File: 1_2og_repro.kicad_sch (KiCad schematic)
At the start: 217 parts, among them J1 Conn_01x03, J2 USB_B_Mini, J3 Conn_01x03, Q1 2N7002, SW1 MX_SW_solder, SW10 MX_SW_solder, SW11 MX_SW_solder, SW12 MX_SW_solder, SW13 MX_SW_solder, SW14 MX_SW_solder, SW15 MX_SW_solder, SW16 MX_SW_solder, SW17 MX_SW_solder, SW18 MX_SW_solder, SW19 MX_SW_solder, SW2 MX_SW_solder, SW20 MX_SW_solder, SW21 MX_SW_solder, SW22 MX_SW_solder, SW23 MX_SW_solder, SW24 MX_SW_solder, SW25 MX_SW_solder, SW26 MX_SW_solder, SW27 MX_SW_solder, SW28 MX_SW_solder, SW29 MX_SW_solder, SW3 MX_SW_solder, SW30 MX_SW_solder, SW31 MX_SW_solder, SW32 MX_SW_solder, SW33 MX_SW_solder, SW34 MX_SW_solder, SW35 MX_SW_solder, SW36 MX_SW_solder, SW37 MX_SW_solder, SW38 MX_SW_solder, SW39 MX_SW_solder, SW4 MX_SW_solder, SW40 MX_SW_solder, SW41 MX_SW_solder, SW42 MX_SW_solder, SW43 MX_SW_solder, SW44 MX_SW_solder, SW45 MX_SW_solder, SW46 MX_SW_solder, SW47 MX_SW_solder, SW48 MX_SW_solder, SW49 MX_SW_solder, SW5 MX_SW_solder, SW50 MX_SW_solder, SW51 MX_SW_solder, SW52 MX_SW_solder, SW53 MX_SW_solder, SW54 MX_SW_solder, SW55 MX_SW_solder, SW56 MX_SW_solder, SW57 MX_SW_solder, SW58 MX_SW_solder, SW59 MX_SW_solder, SW6 MX_SW_solder, SW60 MX_SW_solder, SW61 MX_SW_solder, SW62 MX_SW_solder, SW63 MX_SW_solder, SW64 MX_SW_solder, SW65 MX_SW_solder, SW66 MX_SW_solder, SW67 MX_SW_solder, SW68 MX_SW_solder, SW69 MX_SW_solder, SW7 MX_SW_solder, SW70 MX_SW_solder, SW71 MX_SW_solder, SW72 MX_SW_solder, SW73 MX_SW_solder, SW74 MX_SW_solder, SW75 MX_SW_solder, SW76 MX_SW_solder, SW77 MX_SW_solder, SW78 MX_SW_solder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

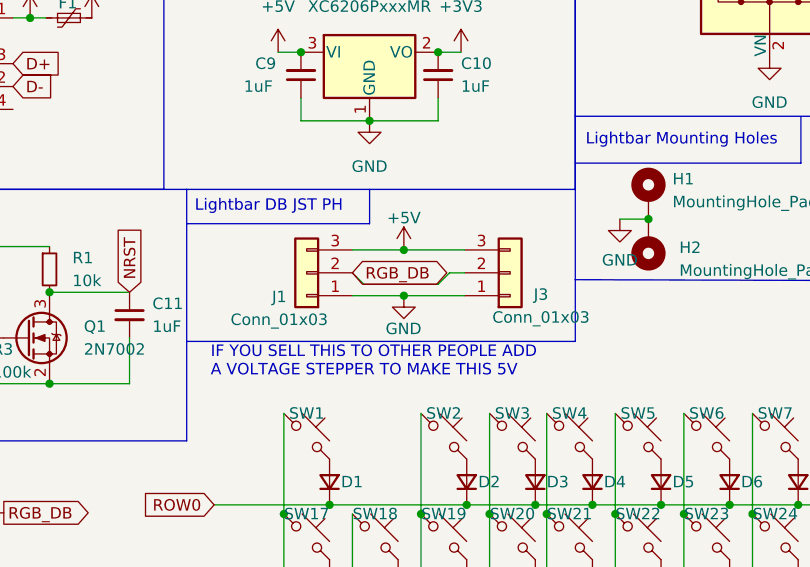
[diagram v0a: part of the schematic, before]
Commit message: add lightbar kinda (gerbers have not been fully updated yet, bom is broken)
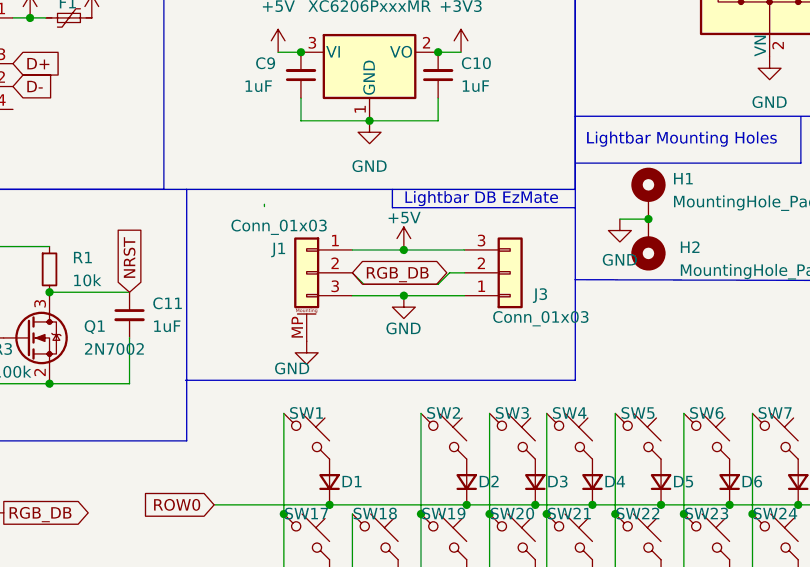
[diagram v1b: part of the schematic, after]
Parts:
- J1: footprint Connector_JST:JST_PH_S3B-PH-K_1x03_P2.00mm_Horizontal -> Connector_Molex:Molex_Pico-EZmate_78171-0003_1x03-1MP_P1.20mm_Vertical; symbol Connector_Generic:Conn_01x03 -> Connector_Generic_MountingPin:Conn_01x03_MountingPin
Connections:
- net +5V: now also J1.1 (Pin_1); no longer J1.3 (Pin_3)
- net GND: now also J1.3 (Pin_3), J1.MP (MountPin); no longer J1.1 (Pin_1)
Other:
- note added: "Lightbar DB EzMate"
- note removed: "IF YOU SELL THIS TO OTHER PEOPLE ADD A VOLTAGE STEPPER TO MAKE THIS 5V"
- note removed: "Lightbar DB JST PH"
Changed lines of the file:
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@@
     (stroke (width 0) (type default))
   )
-  (polyline (pts (xy 156.845 74.676) (xy 156.845 67.818))
+  (polyline (pts (xy 156.845 78.994) (xy 156.845 67.818))
     (stroke (width 0) (type default))
   )
@@
     (stroke (width 0) (type default))
   )
-  (polyline (pts (xy 133.985 61.595) (xy 133.985 57.785))
+  (polyline (pts (xy 136.525 59.817) (xy 136.525 57.785))
     (stroke (width 0) (type default))
   )
@@
     (stroke (width 0) (type default))
   )
-  (polyline (pts (xy 156.845 74.676) (xy 113.665 74.676))
+  (polyline (pts (xy 156.845 78.994) (xy 113.538 78.994))
     (stroke (width 0) (type default))
   )
@@
     (stroke (width 0) (type default))
   )
+  (wire (pts (xy 122.301 59.436) (xy 122.301 59.69))
+    (stroke (width 0) (type default))
+  )
   (wire (pts (xy 80.645 23.495) (xy 90.805 23.495))
     (stroke (width 0) (type default))
@@
     (stroke (width 0) (type default))
   )
-  (polyline (pts (xy 113.665 61.595) (xy 133.985 61.595))
+  (polyline (pts (xy 136.525 59.817) (xy 156.845 59.817))
     (stroke (width 0) (type default))
   )
@@
     (effects (font (size 1.27 1.27)) (justify left bottom))
   )
-  (text "IF YOU SELL THIS TO OTHER PEOPLE ADD\nA VOLTAGE STEPPER TO MAKE THIS 5V"
-    (at 116.332 78.74 0)
-    (effects (font (size 1.27 1.27)) (justify left bottom))
-  )
   (text "Voltage Regulator" (at 112.395 33.655 0)
     (effects (font (size 1.27 1.27)) (justify left bottom))
@@
     (effects (font (size 1.27 1.27)) (justify left bottom))
   )
-  (text "Lightbar DB JST PH" (at 114.554 60.452 0)
+  (text "Lightbar DB EzMate" (at 137.795 59.69 0)
     (effects (font (size 1.27 1.27)) (justify left bottom))
   )
@@
     )
   )
+  (symbol (lib_name "GND_1") (lib_id "power:GND") (at 127 74.676 0) (mirror y) (unit 1)
+    (in_bom yes) (on_board yes) (dnp no)
+    (property "Reference" "#PWR020" (at 127 81.026 0)
+      (effects (font (size 1.27 1.27)) hide)
+    )
+    (property "Value" "GND" (at 127.381 77.724 0)
+      (effects (font (size 1.27 1.27)) (justify left))
+    )
+    (property "Footprint" "" (at 127 74.676 0)
+      (effects (font (size 1.27 1.27)) hide)
+    )
+    (property "Datasheet" "" (at 127 74.676 0)
+      (effects (font (size 1.27 1.27)) hide)
+    )
+    (pin "1")
+    (instances
+      (project "1_2og_repro"
+        (path "/70139223-fff4-476d-a728-a7aa752fc36c"
+          (reference "#PWR020") (unit 1)
+        )
+      )
+      (project "1_2_frl"
+        (path "/a8274e21-5f6e-4c7e-bbe0-133d7f65afea"
+          (reference "#PWR01") (unit 1)
+        )
+      )
+    )
+  )
   (symbol (lib_id "Device:D_Small") (at 219.71 139.573 90) (unit 1)
     (in_bom yes) (on_board yes) (dnp no)
@@
     )
   )
-  (symbol (lib_id "Connector_Generic:Conn_01x03") (at 127 67.056 180) (unit 1)
+  (symbol (lib_id "Connector_Generic_MountingPin:Conn_01x03_MountingPin") (at 127 67.056 0) (mirror y) (unit 1)
     (in_bom yes) (on_board yes) (dnp no)
-    (property "Reference" "J1" (at 123.952 69.723 0)
+    (property "Reference" "J1" (at 123.952 64.389 0)
       (effects (font (size 1.27 1.27)))
     )
-    (property "Value" "Conn_01x03" (at 123.952 72.263 0)
+    (property "Value" "Conn_01x03" (at 123.952 61.849 0)
       (effects (font (size 1.27 1.27)))
     )
-    (property "Footprint" "Connector_JST:JST_PH_S3B-PH-K_1x03_P2.00mm_Horizontal" (at 127 67.056 0)
+    (property "Footprint" "Connector_Molex:Molex_Pico-EZmate_78171-0003_1x03-1MP_P1.20mm_Vertical" (at 127 67.056 0)
       (effects (font (size 1.27 1.27)) hide)
     )
@@
     (pin "2")
     (pin "3")
+    (pin "MP")
     (instances
       (project "1_2og_repro"

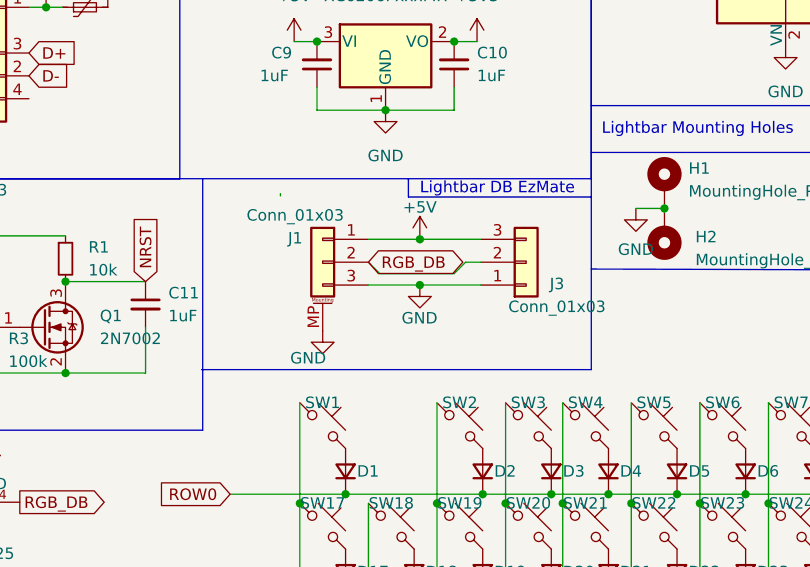
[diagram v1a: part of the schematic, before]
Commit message: dual jst-ph and ezmate support on pcb
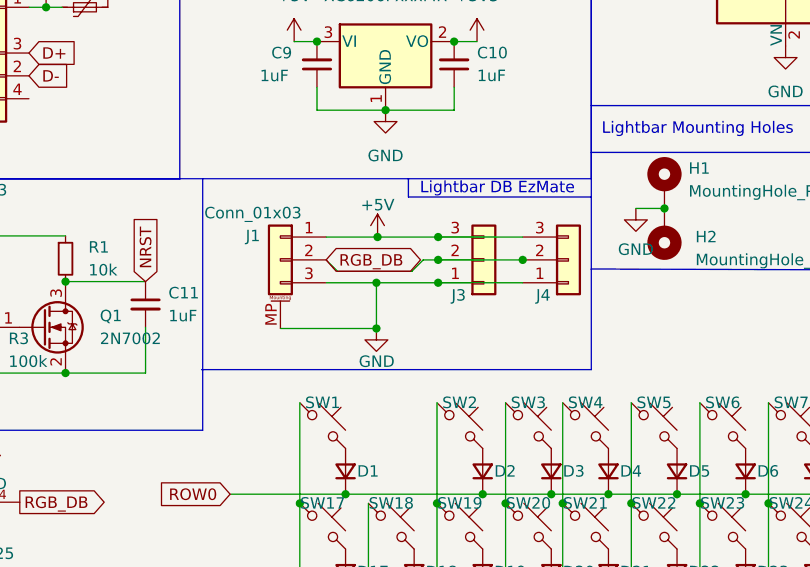
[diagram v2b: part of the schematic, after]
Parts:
- added J4: Conn_01x03, Connector_JST:JST_PH_S3B-PH-K_1x03_P2.00mm_Horizontal, symbol Connector_Generic:Conn_01x03
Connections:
- net +5V: now also J4.3 (Pin_3)
- net GND: now also J4.1 (Pin_1)
- net RGB_DB: now also J4.2 (Pin_2)
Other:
- moved on the sheet: J1, J3
